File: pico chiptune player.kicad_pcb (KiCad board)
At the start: 4 copper layers, 80 x 70.8 mm, 31 parts, among them J1 Speaker Out, J2 MicroSD, SW1 Play / Pause, SW2 Next, SW3 Previous, U1 AY-3-8910, U2 0.96"OLED_I2C, U3 PAM8302AAS

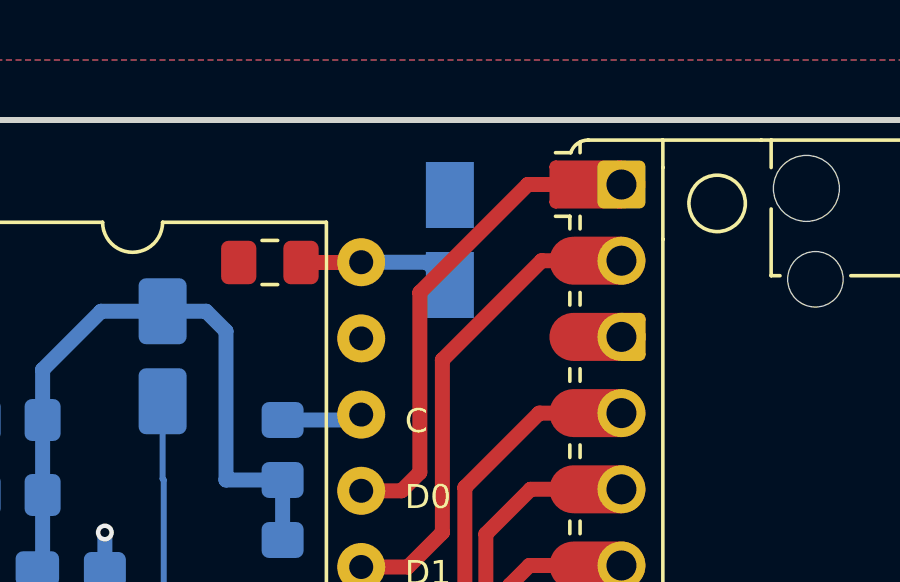
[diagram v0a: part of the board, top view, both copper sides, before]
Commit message: sch, bom: add LCSC Part # numbers for JLCPCB SMT PCBA assembly
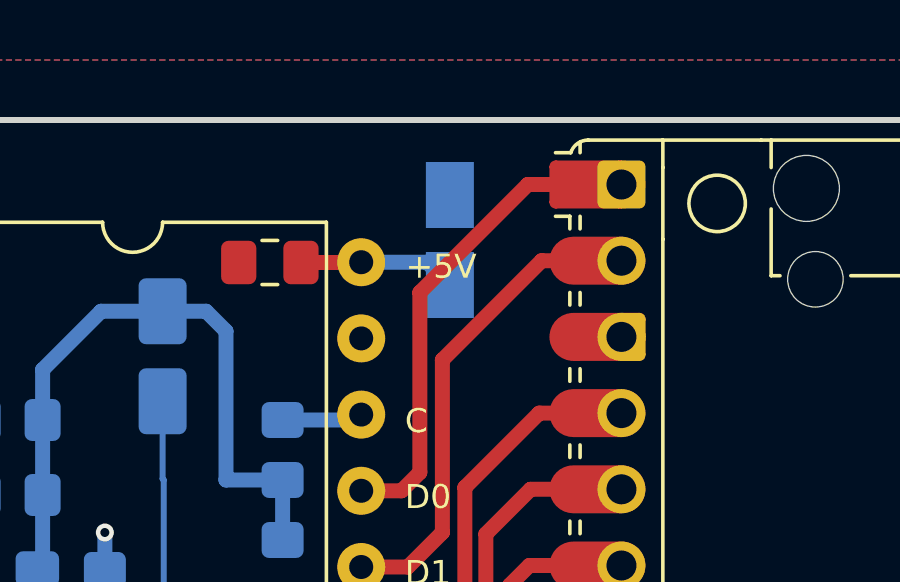
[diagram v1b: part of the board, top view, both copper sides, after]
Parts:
- J1: value Speaker Out -> Spk Out
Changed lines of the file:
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@@
 			)
 		)
-		(property "Value" "Speaker Out"
-			(at -0.5 1.5 0)
+		(property "Value" "Spk Out"
+			(at -0.5 1.75 0)
 			(layer "B.SilkS")
 			(effects
@@
 		)
 		(property "Value" "10uF"
-			(at -4.25 2.25 90)
+			(at 0.25 3 90)
 			(layer "B.SilkS")
 			(effects
@@
 		(layer "F.SilkS")
 		(effects
+			(font
+				(size 0.8 0.8)
+				(thickness 0.15)
+			)
+			(justify left bottom)
+		)
+	)
+	(gr_text "+5V"
+		(at 128.525 77.855 0)
+		(layer "F.SilkS")
+		(effects

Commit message: fix: update DNP option in fabrication toolkit and correct netlist references
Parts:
- J1: value Spk Out -> Speaker Out
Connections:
- R2 pad 2: Net-(A1-GPIO11) -> Net-(R2-Pad2)
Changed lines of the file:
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@@
 			)
 		)
-		(property "Value" "Spk Out"
+		(property "Value" "Speaker Out"
 			(at -0.5 1.75 0)
 			(layer "B.SilkS")
@@
 			(layers "F.Cu" "F.Mask" "F.Paste")
 			(roundrect_rratio 0.208333)
-			(net "Net-(A1-GPIO11)")
+			(net "Net-(R2-Pad2)")
 			(pintype "passive")
 		)

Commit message: Refactor code structure for improved readability and maintainability
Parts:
- removed J1: Speaker Out, Connector_PinSocket_1.27mm:PinSocket_2x01_P1.27mm_Vertical
- removed R6: 10K, Resistor_SMD:R_0805_2012Metric_Pad1.20x1.40mm_HandSolder
- removed RV1: 3224W-1-103E, Potentiometer_SMD:Potentiometer_Bourns_3224W_Vertical
- added C6: 10uF, Capacitor_SMD:CP_Elec_4x5.4, F.Cu at (181.0, 104.2)
- added C7: 100nF, Capacitor_SMD:C_0805_2012Metric_Pad1.18x1.45mm_HandSolder, F.Cu at (175.6, 102.8)
- added C8: 100nF, Capacitor_SMD:C_0805_2012Metric_Pad1.18x1.45mm_HandSolder, B.Cu at (123.2, 74.2)
- added G***: LOGO, LOGO, B.Cu at (173.0, 107.4)
- A1: footprint Module_RaspberryPi_Pico:RaspberryPi_Pico_Common -> TMCu Module:RPi_Pico_SMD_TH
- C1: footprint Capacitor_SMD:CP_Elec_3x5.3 -> Capacitor_SMD:CP_Elec_4x5.4
- C4, C5: value 10nF -> 100nF
- J2: footprint terence:MicroSD -> Terence:MicroSD
- JP1: moved to F.Cu
- U2: footprint terence:0.96OLED I2C -> TModules:OLED 0.96 I2C
- U3: value PAM8302AAS -> PAM8302; footprint Package_SO:SOIC-8_3.9x4.9mm_P1.27mm -> TModules:PAM8302A_Module; moved to F.Cu
- moved U3 29.3 mm to (119.4, 65.7)
- moved G*** 25.7 mm to (146.2, 130.4)
- moved SW3 25.1 mm to (142.2, 132.7), turned to 180 degrees
- moved G*** 19.9 mm to (139.0, 130.4)
- moved G*** 17.5 mm to (166.4, 130.7)
- moved SW1 17.0 mm to (162.5, 132.7), turned to 180 degrees
- moved G*** 12.4 mm to (159.3, 130.4), turned to 0 degrees
- moved SW2 9.12 mm to (182.8, 132.6), turned to 180 degrees
- moved G*** 7.28 mm to (179.6, 130.3)
- moved JP1 6.65 mm to (122.3, 118.0)
- moved R3 6.43 mm to (123.6, 125.7), turned to 180 degrees
- moved C4 5.74 mm to (120.6, 84.8), turned to 90 degrees
- moved R2 5.45 mm to (132.0, 122.4)
- moved C3 5.44 mm to (115.9, 83.4), turned to 180 degrees
- moved U1 5.25 mm to (111.8, 82.5)
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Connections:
- A1 pad 11: /BDIR -> /BC1
- A1 pad 12: /BC1 -> /SD_Amp
- A1 pad 14: /~{RESET} -> /BDIR
- A1 pad 15: Net-(A1-GPIO11) -> /~{RESET}
- A1 pad 16: /SW_PREV -> Net-(A1-GPIO12)
- A1 pad 17: /SW_PLAY -> /SW_NEXT
- A1 pad 19: unconnected-(A1-GPIO14-Pad19) -> /SW_PLAY
- A1 pad 20: /SW_NEXT -> /SW_PREV
- C3 pad 2: Net-(C3-Pad2) -> Net-(U3-A+)
- R2 pad 2: Net-(R2-Pad2) -> Net-(A1-GPIO12)
- U3 pad 1: Net-(U3-~{SD}) -> GND
- U3 pad 2: unconnected-(U3-NC-Pad2) -> +5V
- U3 pad 3: Net-(U3-IN+) -> /SD_Amp
- U3 pad 5: Net-(J1-Pin_2) -> Net-(U3-A+)
- U3 pad 6: +5V -> unconnected-(U3-OUT+-Pad6)
- U3 pad 7: GND -> unconnected-(U3-OUT--Pad7)
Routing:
- net /SD_Amp: track 0.00 -> 56.9 mm
- net +3.3V: track 40.6 -> 78.9 mm
- net GND: track 0.63 -> 34.6 mm, vias 10 -> 11
- net Net-(C3-Pad2): track 25.7 -> 0.00 mm
- net /SW_PREV: track 38.7 -> 19.1 mm
- net Net-(A1-GPIO12): track 0.00 -> 11.8 mm
- net Net-(U3-IN+): track 11.8 -> 0.00 mm
- net +5V: track 9.11 -> 20.5 mm, vias 2 -> 0
- net Net-(J1-Pin_2): track 10.7 -> 0.00 mm
- net Net-(A1-GPIO11): track 9.36 -> 0.00 mm
- net Net-(U3-~{SD}): track 8.64 -> 0.00 mm
- net /SW_NEXT: track 52.5 -> 60.1 mm
- net Net-(U3-A+): track 0.00 -> 7.24 mm
- net Net-(C3-Pad1): track 22.8 -> 15.7 mm
- net /BC1: track 9.75 -> 16.0 mm
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- removed copper zone on B.Cu, net GND
- removed copper zone on F.Cu, net GND
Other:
- board size 80 x 70.8 mm -> 80 x 62.4 mm
- board text added: "14082026"
- board text added: "Terence Ang / MotionFxDesign"
- board text added: "YM2149F"
- board text added: "YM2419F"
- board text added: "https://github.com/terenceang/pico-chiptune-player"
- board text removed: "Terence Ang / MotionFxDesign 2026"
- board text removed: "VOL"

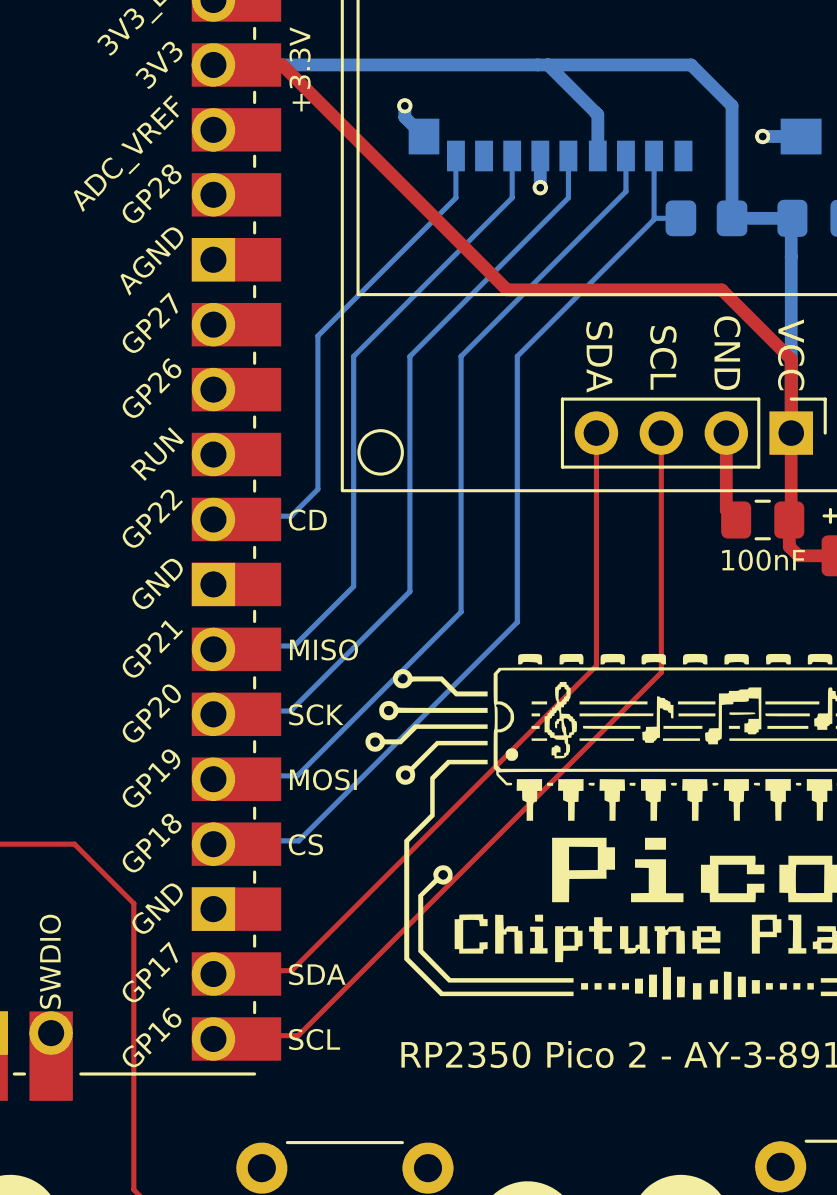
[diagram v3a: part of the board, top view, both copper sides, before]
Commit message: sch, pcb, docs: update to Rev 0.5 native-compliant SD/OLED pinout
Remap RP2350 peripherals to their native pins: OLED SDA=GP16/SCL=GP17, SD SCK=GP18/MOSI=GP19/MISO=GP20/CS=GP21 (card detect stays GP22).

- Schematic: swap OLED SDA/SCL labels, remap SD SPI labels, move R1 pull-up back onto SD_CS; retitle to 0.5
- PCB: resync A1 pads, reroute the 5 affected nets (0 unconnected), refill zones, retitle to 0.5; DRC unchanged from Rev 0.4
- Docs: HARDWARE.md/README.md/VERSION set as Rev 0.5 SSOT with errata
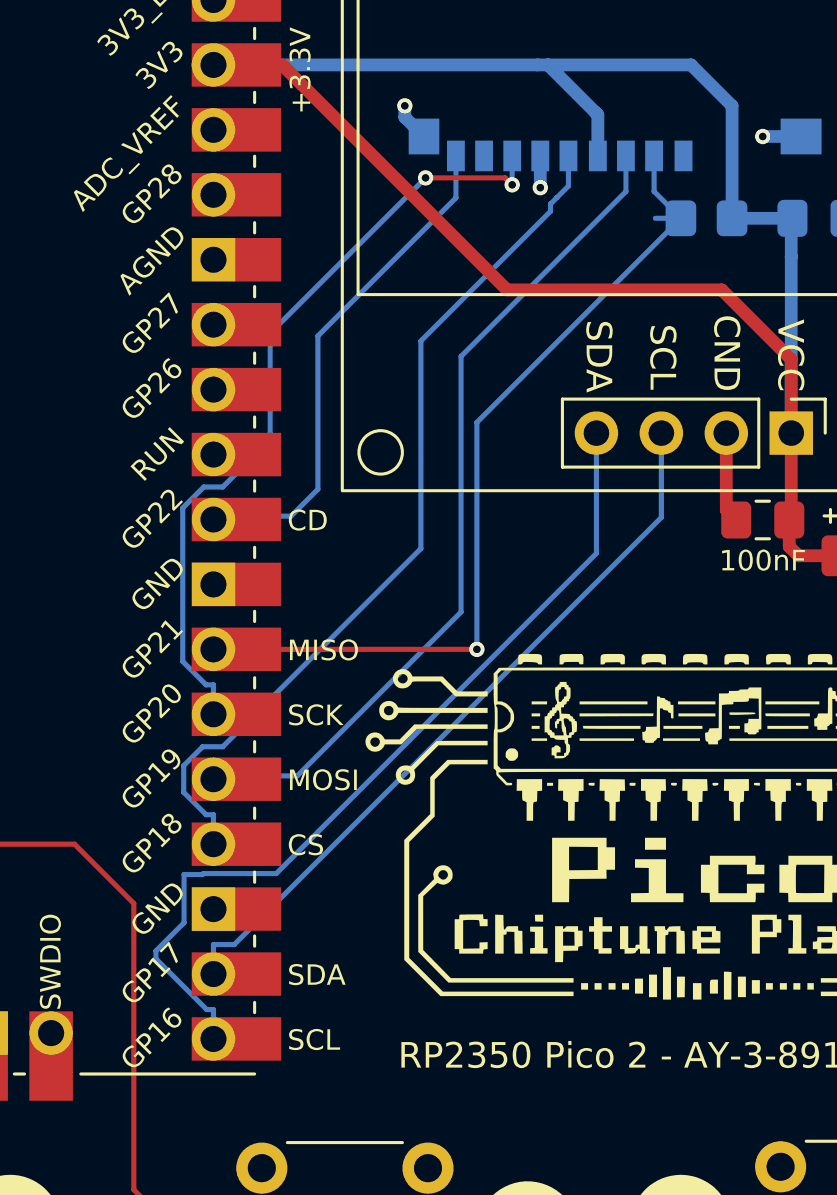
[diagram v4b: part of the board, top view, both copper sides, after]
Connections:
- A1 pad 21: /OLED_SCL -> /OLED_SDA
- A1 pad 22: /OLED_SDA -> /OLED_SCL
- A1 pad 24: /SD_CS -> /SD_SCK
- A1 pad 26: /SD_SCK -> /SD_MISO
- A1 pad 27: /SD_MISO -> /SD_CS
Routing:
- net /OLED_SCL: track 33.4 -> 28.9 mm
- net /SD_SCK: track 29.8 -> 34.3 mm
- net /OLED_SDA: track 29.6 -> 34.0 mm
- net /SD_MISO: track 26.5 -> 30.6 mm, vias 0 -> 2
- net /SD_CS: track 36.5 -> 33.3 mm, vias 0 -> 1

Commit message: pcb: harden PDN with +3.3V B.Cu pour and power stitching vias
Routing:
- net GND: vias 11 -> 14
- net +5V: vias 0 -> 1
- net +3.3V: vias 0 -> 5
- added copper zone on B.Cu, net +3.3V
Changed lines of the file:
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@@
+	)
+	(via
+		(at 174.175 100.906761)
+		(size 0.6)
+		(drill 0.3)
+		(layers "F.Cu" "B.Cu")
+		(net "GND")
 	)
 	(via
@@
 	)
 	(via
+		(at 124.46 77.74875)
+		(size 0.6)
+		(drill 0.3)
+		(layers "F.Cu" "B.Cu")
+		(net "GND")
+	)
+	(via
 		(at 183.8 105.6)
+		(size 0.6)
+		(drill 0.3)
+		(layers "F.Cu" "B.Cu")
+		(net "GND")
+	)
+	(via
+		(at 127.13 76.2)
 		(size 0.6)
 		(drill 0.3)
@@
 		(net "+3.3V")
 	)
+	(via
+		(at 175.3575 95.1575)
+		(size 0.6)
+		(drill 0.3)
+		(layers "F.Cu" "B.Cu")
+		(net "+3.3V")
+	)
+	(via
+		(at 176.715 101.061761)
+		(size 0.6)
+		(drill 0.3)
+		(layers "F.Cu" "B.Cu")
+		(net "+3.3V")
+	)
+	(via
+		(at 155.4575 85)
+		(size 0.6)
+		(drill 0.3)
+		(layers "F.Cu" "B.Cu")
+		(net "+3.3V")
+	)
+	(via
+		(at 161.2 89.4)
+		(size 0.6)
+		(drill 0.3)
+		(layers "F.Cu" "B.Cu")
+		(net "+3.3V")
+	)
+	(via
+		(at 176.715 97.958011)
+		(size 0.6)
+		(drill 0.3)
+		(layers "F.Cu" "B.Cu")
+		(net "+3.3V")
+	)
 	(segment
 		(start 167.2 85)
@@
 		(net "+5V")
 	)
+	(via
+		(at 121.92 78.86)
+		(size 0.6)
+		(drill 0.3)
+		(layers "F.Cu" "B.Cu")
+		(net "+5V")
+	)
 	(segment
 		(start 121.92 74.52)
@@
 	)
 	(zone
+		(net "+3.3V")
+		(layer "B.Cu")
+		(hatch edge 0.5)
+		(connect_pads
+			(clearance 0.3)
+		)
+		(min_thickness 0.25)
+		(fill yes
+			(thermal_gap 0.5)
+			(thermal_bridge_width 0.5)
+			(island_removal_mode 0)
+		)
+		(polygon
+			(pts
+				(xy 104 70.5) (xy 191.5 70.5) (xy 192.033111 150.999811) (xy 104.532894 151.499812)
+			)
+		)
+	)
+	(zone

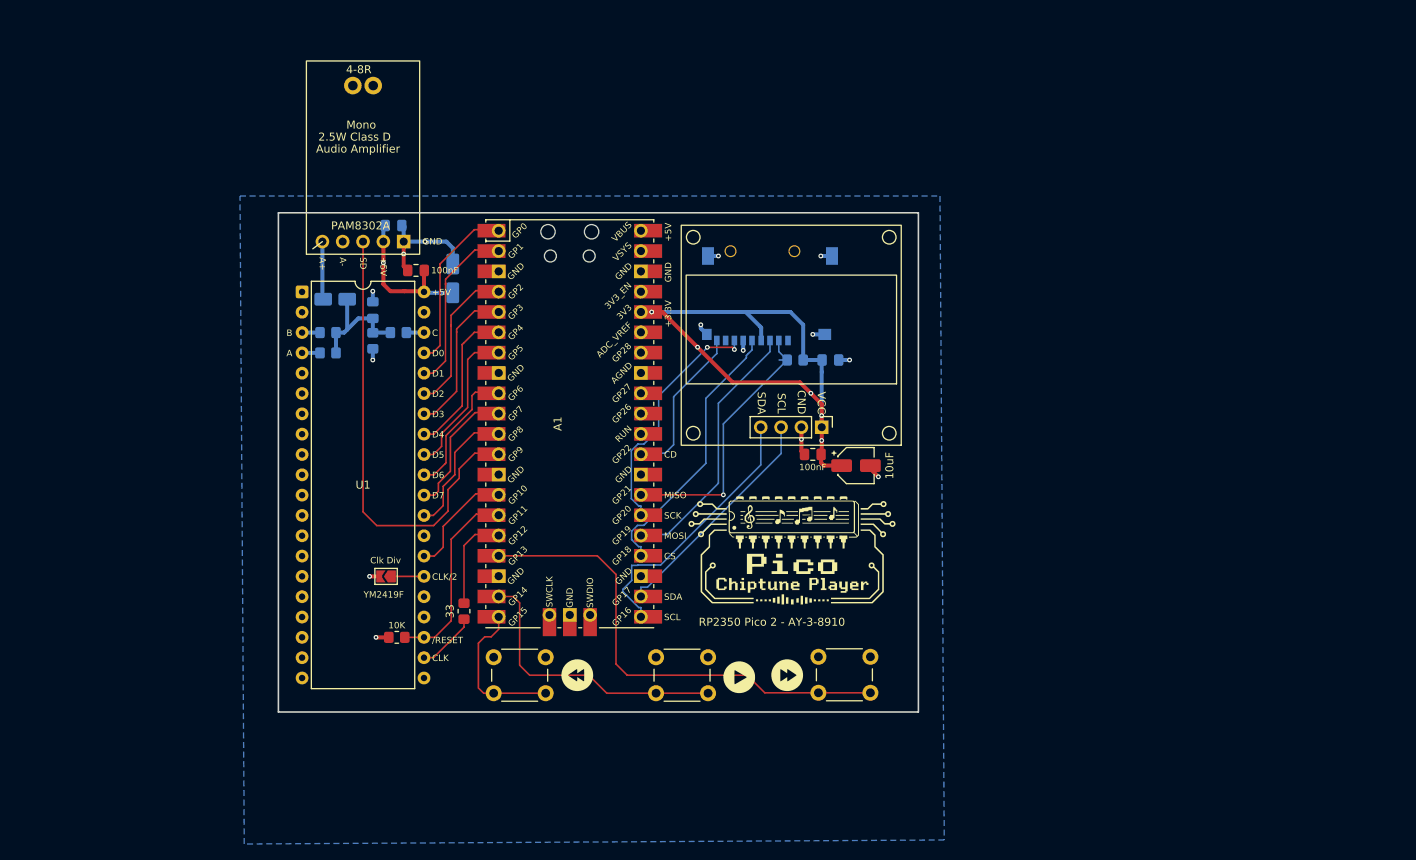
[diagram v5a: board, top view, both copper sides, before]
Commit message: sch, pcb, docs: dual YM2149 stereo variant (Rev 0.6)
- Add second PSG (U4) sharing DA0..7/CLOCK/~RESET/BC2, driven by
  dedicated BDIR2 (GPIO26) and BC1_2 (GPIO27) for 6 voices total
- Add right-channel passive mixer (R9-R12, C9, C10) and second
  PAM8302A amp module (U5) with decoupling (C11-C13) for stereo
- Widen board to 139.4 x 62.6 mm; autoroute with Freerouting
  (0 unconnected items, ERC 0 errors)
- Update HARDWARE.md/README.md/VERSION to Rev 0.6
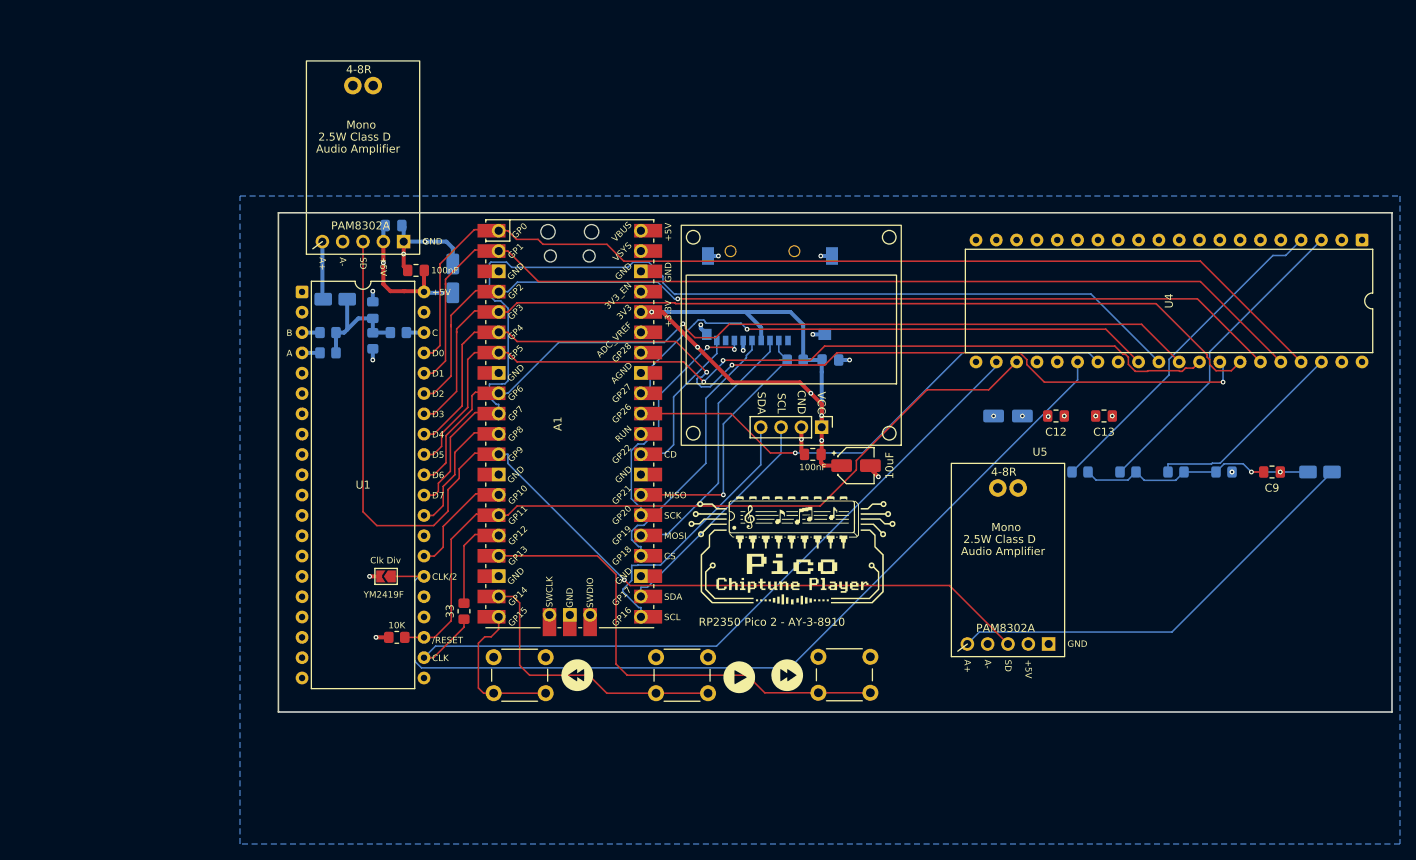
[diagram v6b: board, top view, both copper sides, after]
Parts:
- added C10: 1uF, Capacitor_SMD:CP_Elec_3x5.4, B.Cu at (239.0, 105.0)
- added C11: 10uF, Capacitor_SMD:CP_Elec_4x5.4, B.Cu at (200.0, 98.0)
- added C12: 100nF, Capacitor_SMD:C_0805_2012Metric_Pad1.18x1.45mm_HandSolder, F.Cu at (206.0, 98.0)
- added C13: 100nF, Capacitor_SMD:C_0805_2012Metric_Pad1.18x1.45mm_HandSolder, F.Cu at (212.0, 98.0)
- added C9: 100nF, Capacitor_SMD:C_0805_2012Metric_Pad1.18x1.45mm_HandSolder, F.Cu at (233.0, 105.0)
- added R10: 1k, Resistor_SMD:R_0805_2012Metric_Pad1.20x1.40mm_HandSolder, B.Cu at (215.0, 105.0)
- added R11: 1k, Resistor_SMD:R_0805_2012Metric_Pad1.20x1.40mm_HandSolder, B.Cu at (221.0, 105.0)
- added R12: 1k, Resistor_SMD:R_0805_2012Metric_Pad1.20x1.40mm_HandSolder, B.Cu at (227.0, 105.0)
- added R9: 1k, Resistor_SMD:R_0805_2012Metric_Pad1.20x1.40mm_HandSolder, B.Cu at (209.0, 105.0)
- added U4: YM2149F, Package_DIP:DIP-40_W15.24mm, F.Cu at (244.3, 76.0)
- added U5: PAM8302, TModules:PAM8302A_Module, F.Cu at (200.0, 116.0)
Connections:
- net Net-(JP1-A) renamed /JP1_SEL
- A1 pad 31: unconnected-(A1-GPIO26_ADC0-Pad31) -> /BDIR2
- A1 pad 32: unconnected-(A1-GPIO27_ADC1-Pad32) -> /BC1_2
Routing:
- net /DA7: track 16.1 -> 129.6 mm
- net /JP1_SEL: track 4.72 -> 115.9 mm
- net /DA0: track 21.1 -> 128.8 mm
- net /DA1: track 21.3 -> 125.4 mm
- net /DA4: track 19.1 -> 121.5 mm, vias 0 -> 3
- net /DA2: track 18.7 -> 119.2 mm, vias 0 -> 1
- net /DA3: track 18.8 -> 117.1 mm
- net /DA5: track 19.0 -> 112.6 mm, vias 0 -> 2
- net /DA6: track 16.0 -> 108.8 mm, vias 0 -> 1
- net /CLOCK: track 7.58 -> 94.8 mm
- net /SD_Amp: track 56.9 -> 131.7 mm, vias 0 -> 1
- net /~{RESET}: track 23.6 -> 97.6 mm
- net /BC1_2: track 0.00 -> 70.1 mm, vias 0 -> 1
- net /BDIR2: track 0.00 -> 64.8 mm, vias 0 -> 1
- net /AMP2_IN: track 0.00 -> 54.5 mm
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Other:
- board size 80 x 62.4 mm -> 139.2 x 62.4 mm
